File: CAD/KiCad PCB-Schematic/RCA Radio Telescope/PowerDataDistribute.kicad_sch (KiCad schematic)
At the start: 2 parts, among them J1 USB_A, J3 USB_A

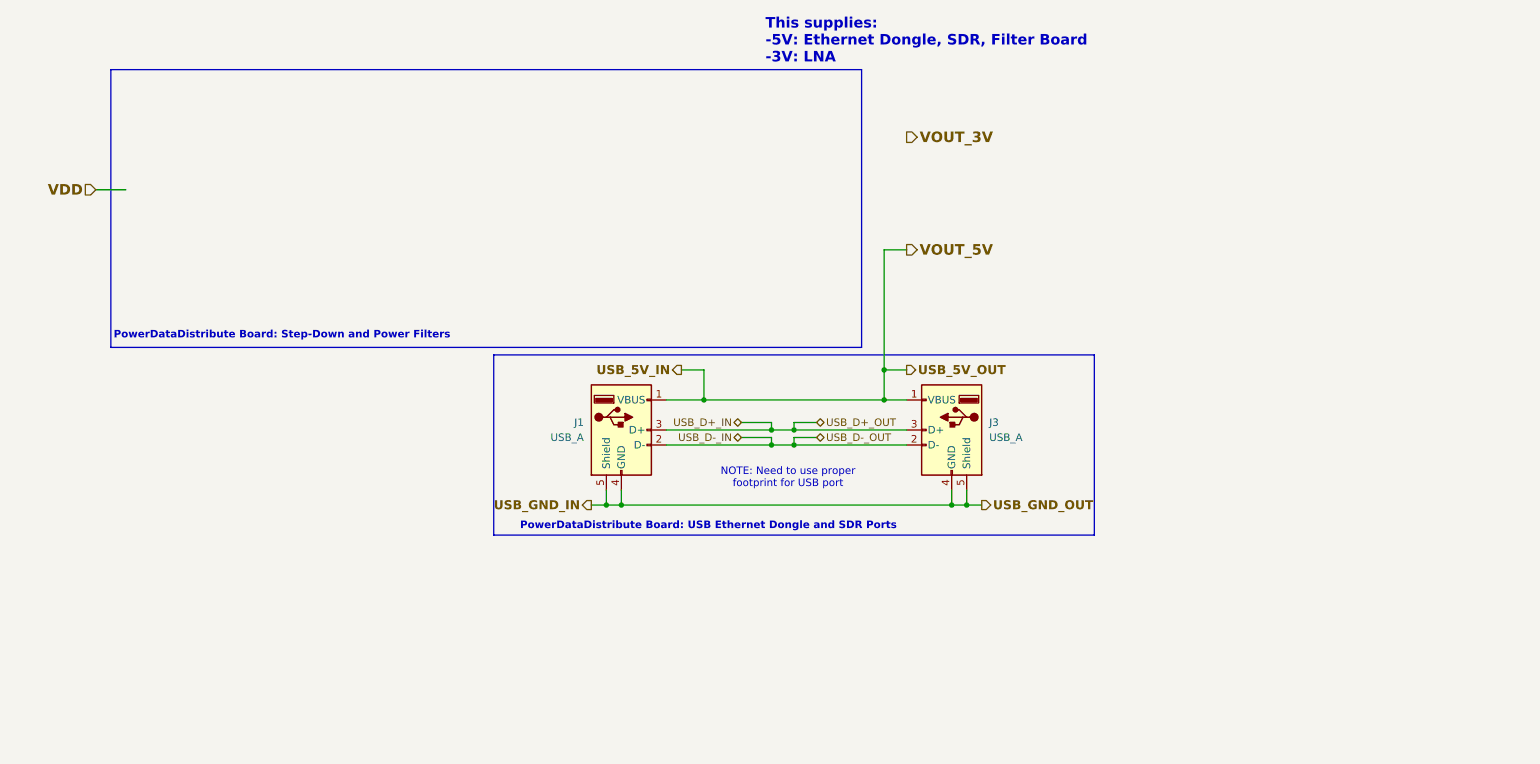
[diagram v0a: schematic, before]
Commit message: Updated Schematic
Updated Root Schematic to v1.4
- Added Screw Terminals for 5V In/Out, 3V Out for LNA
- Reorganized Skylark Shed Power to include Battery, Inverter, and AC-DC Adapter
- Added TODO list

Updated PowerDataDistribute Schematic to v1.1
- Removed labels for USB signals and replaced it with single USB_OUT signal
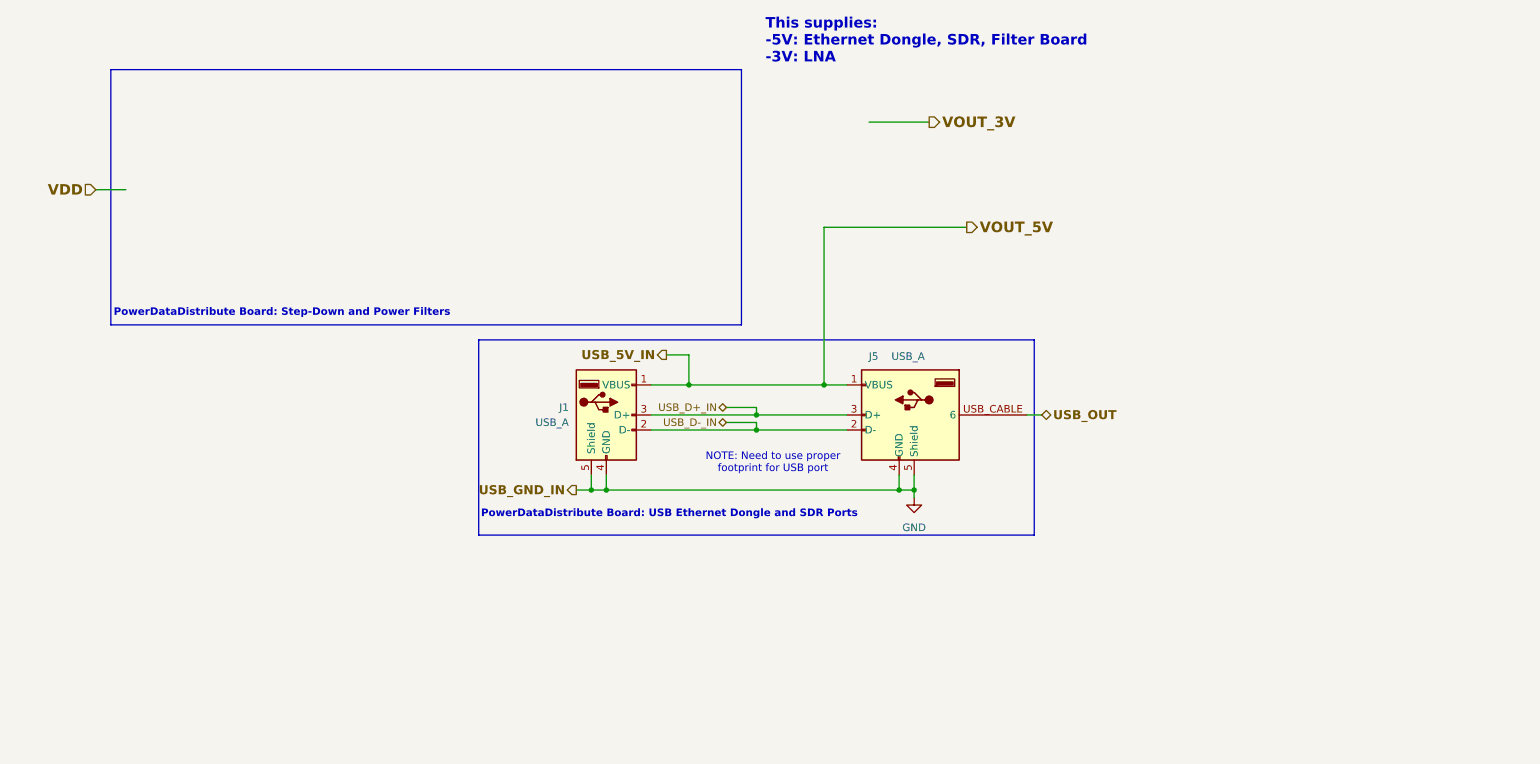
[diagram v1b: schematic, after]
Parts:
- removed J3: USB_A, symbol Connector:USB_A
- added J5: USB_A, symbol Radio Telescope:USB_A_WIRED
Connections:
- net USB_5V_IN: now also J5.1 (VBUS)
- net USB_D+_IN: now also J5.3 (D+)
- net USB_D-_IN: now also J5.2 (D-)
- net USB_GND_IN renamed GND
- net GND: now also J5.4 (GND), J5.5 (Shield)
- new net USB_OUT: J5.USB_CABLE (6)
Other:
- moved on the sheet: J1

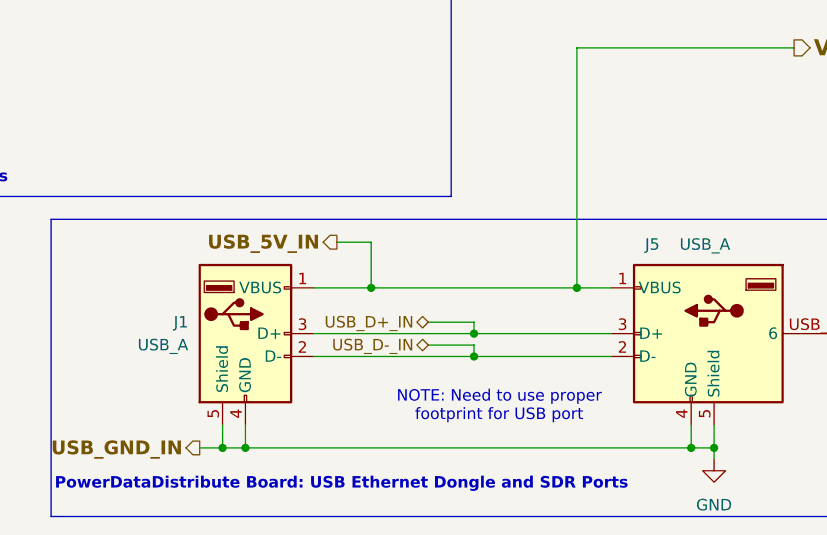
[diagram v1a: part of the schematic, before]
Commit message: Updated Schematic
Updated Root Schematic to v1.5, Filters to v1.1, and PowerDataDistribute to v1.1.
- Updated part references to be more consistent
- Added missing GND label for SDR GPO
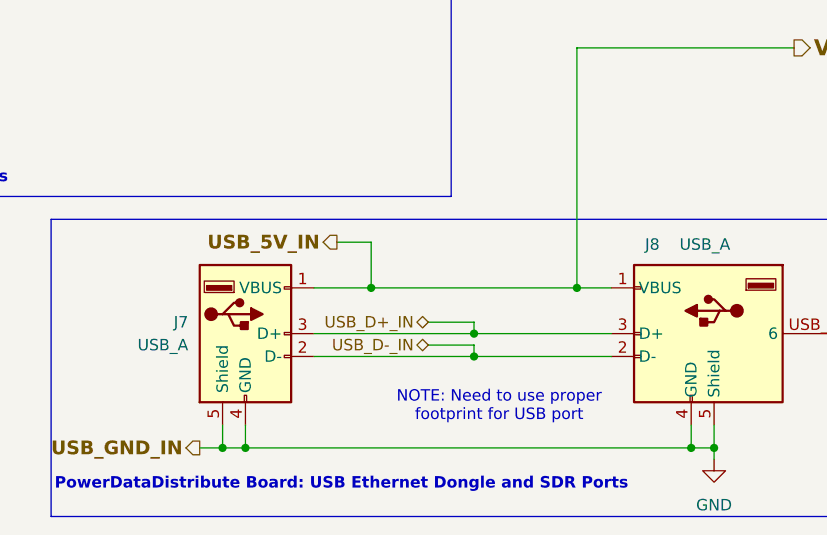
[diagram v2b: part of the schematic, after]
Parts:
- renumbered J1 to J7, J5 to J8
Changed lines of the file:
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@@
 	(title_block
 		(title "PowerDataDistribute")
-		(rev "Version 1.1")
+		(rev "Version 1.2")
 	)
 	(junction
@@
 		(on_board yes)
 		(dnp no)
-		(property "Reference" "J5"
+		(property "Reference" "J8"
 			(at 156.972 71.374 0)
 			(effects
@@
 			(project ""
 				(path "/1630c5ee-b70a-455e-85ba-86a73955b8fd/27e6aa46-cfac-490f-80c1-5c0f7cb6c2e8"
-					(reference "J5")
+					(reference "J8")
 					(unit 1)
 				)
@@
 		(on_board yes)
 		(dnp no)
-		(property "Reference" "J1"
+		(property "Reference" "J7"
 			(at 105.41 80.0099 0)
 			(effects
@@
 			(project ""
 				(path "/1630c5ee-b70a-455e-85ba-86a73955b8fd/27e6aa46-cfac-490f-80c1-5c0f7cb6c2e8"
-					(reference "J1")
+					(reference "J7")
 					(unit 1)
 				)

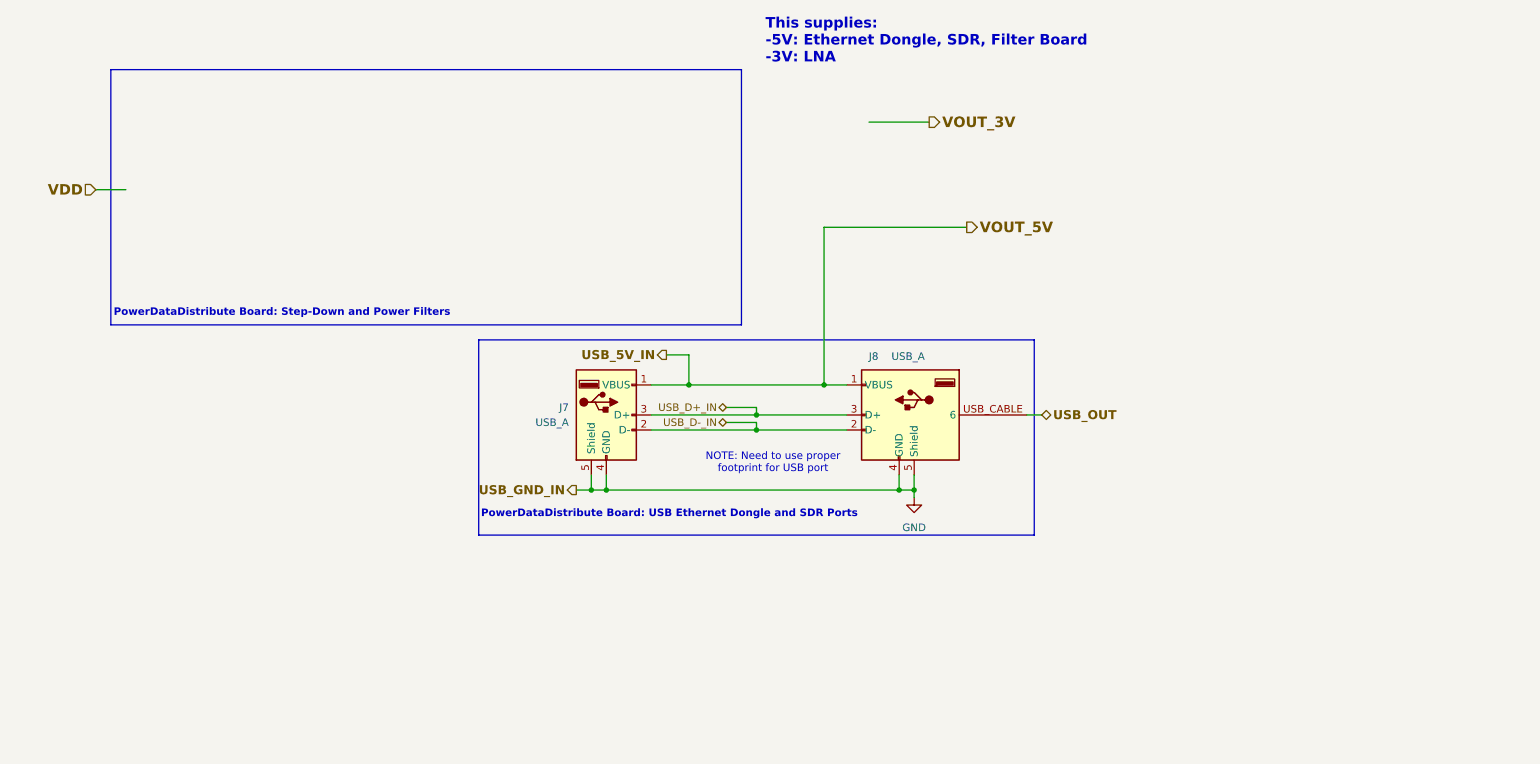
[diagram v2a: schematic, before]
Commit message: Updated PowerDataDistribute Schematic to v1.3
- Added 5V to 3V Buck for LNA
- Added TVS diode, PMOS, and polyfuse for power protection (need to select PMOS and polyfuse)
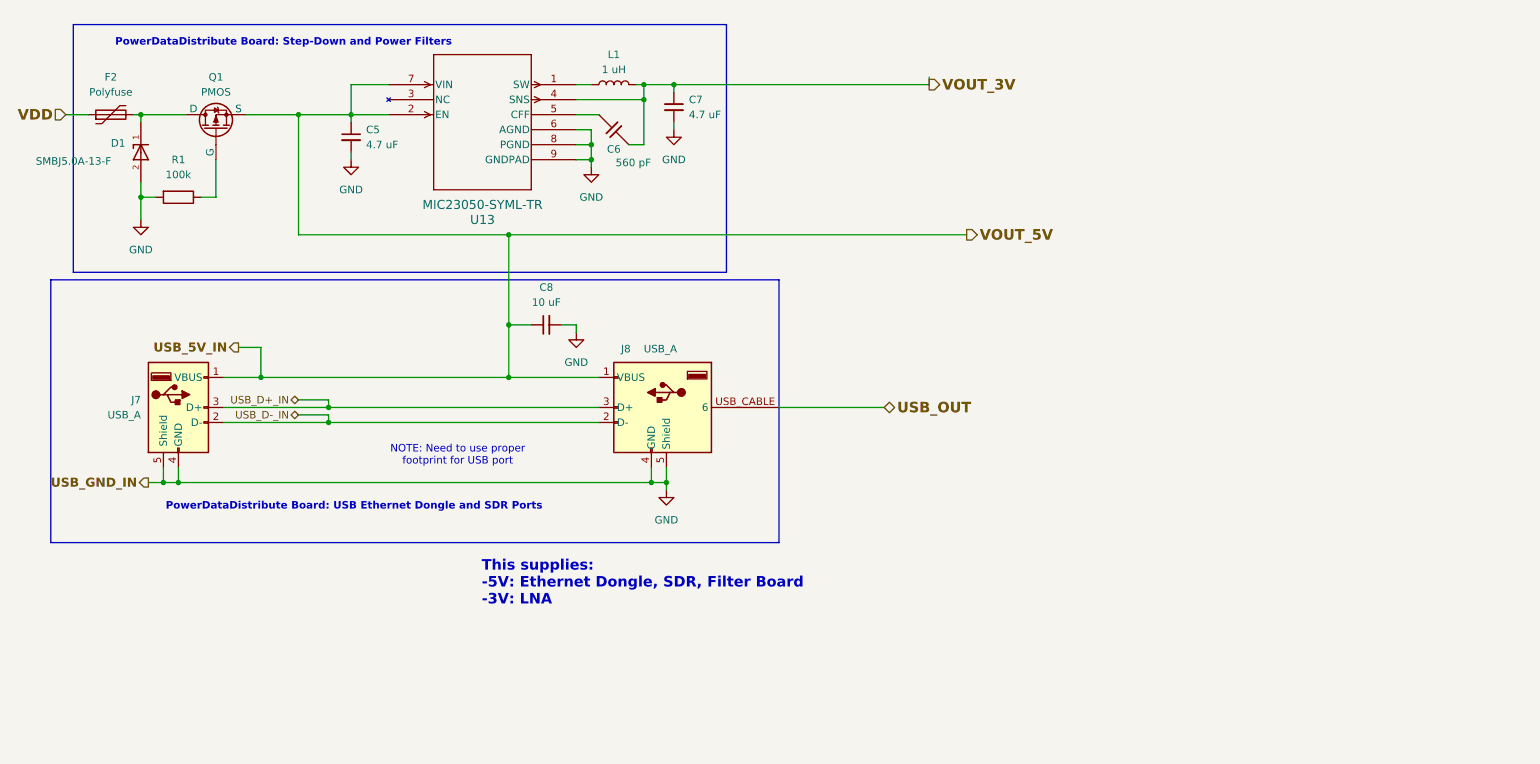
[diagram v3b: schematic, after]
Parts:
- added C5, C7: 4.7 uF, symbol Device:C_Small
- added C6: 560 pF, symbol Device:C_45deg
- added C8: 10 uF, symbol Device:C_Small
- added D1: SMBJ5.0A-13-F, SMBJ5.0A-13-F:DIOM5336X250N, symbol Radio Telescope:SMBJ5.0A-13-F
- added F2: Polyfuse, symbol Device:Polyfuse
- added L1: 1 uH, symbol Device:L
- added Q1: PMOS, symbol Simulation_SPICE:PMOS
- added R1: 100k, symbol Device:R
- added U13: MIC23050-SYML-TR, MLF-8_ML_MCH, symbol Radio Telescope:MIC23050-SYML-TR
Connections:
- net GND: now also C5.2, C7.2, C8.2, D1.2, R1.2, U13.6 (AGND), U13.8 (PGND), U13.9 (GNDPAD)
- net USB_5V_IN: now also C5.1, C8.1, Q1.3 (S), U13.2 (EN), U13.7 (VIN)
- net VDD: now also F2.1
- net VOUT_3V: now also C6.1, C7.1, L1.2, U13.4 (SNS)
- new net: D1.1, F2.2, Q1.1 (D)
- new net: C6.2, U13.5 (CFF)
- new net: L1.1, U13.1 (SW)
- new net: Q1.2 (G), R1.1
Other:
- moved on the sheet: J7, J8
